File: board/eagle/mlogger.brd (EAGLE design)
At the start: 59.4 x 33.3 mm, 40 parts, among them J1 MICROSD-9P, SW1 SS-12D00G3, SW2 TVAF06-A020B-R, SW3 TVAF06-A020B-R

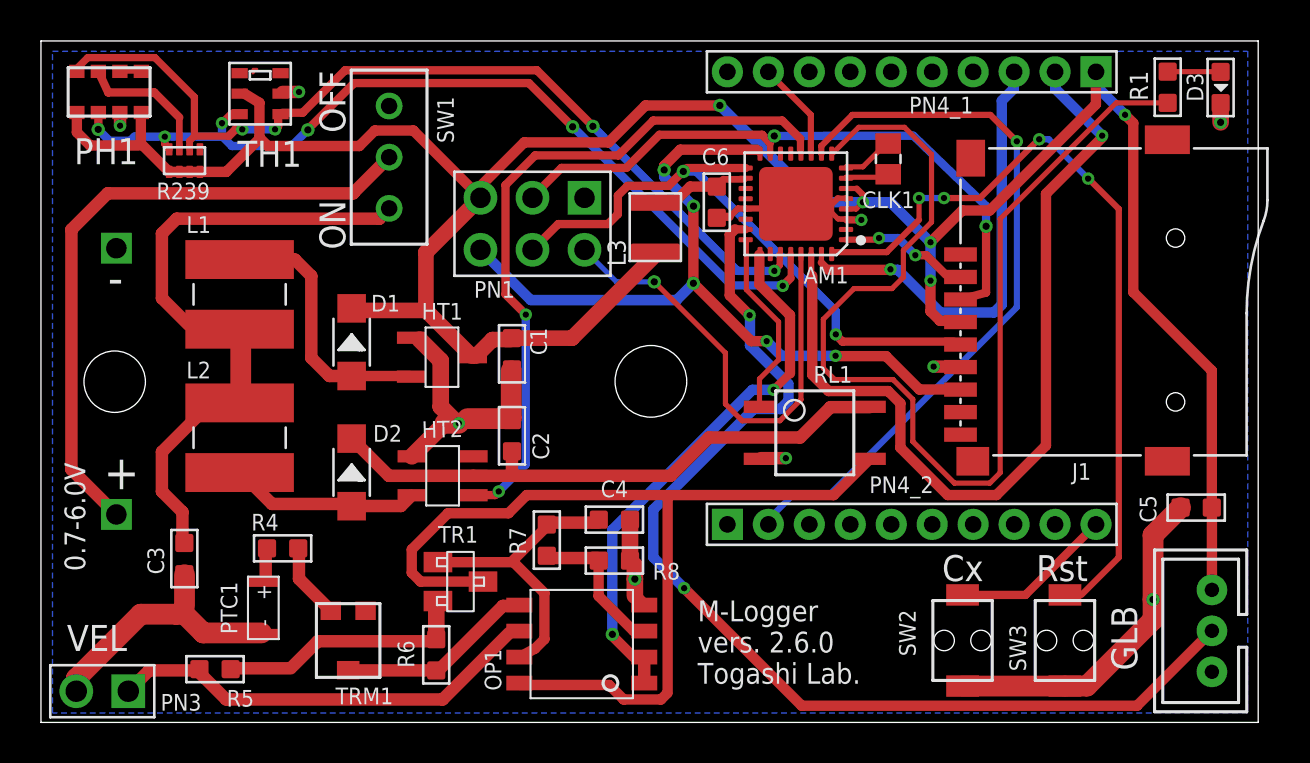
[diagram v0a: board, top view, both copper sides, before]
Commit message: AVR32DB32を使ったVersion3.0の開発開始。
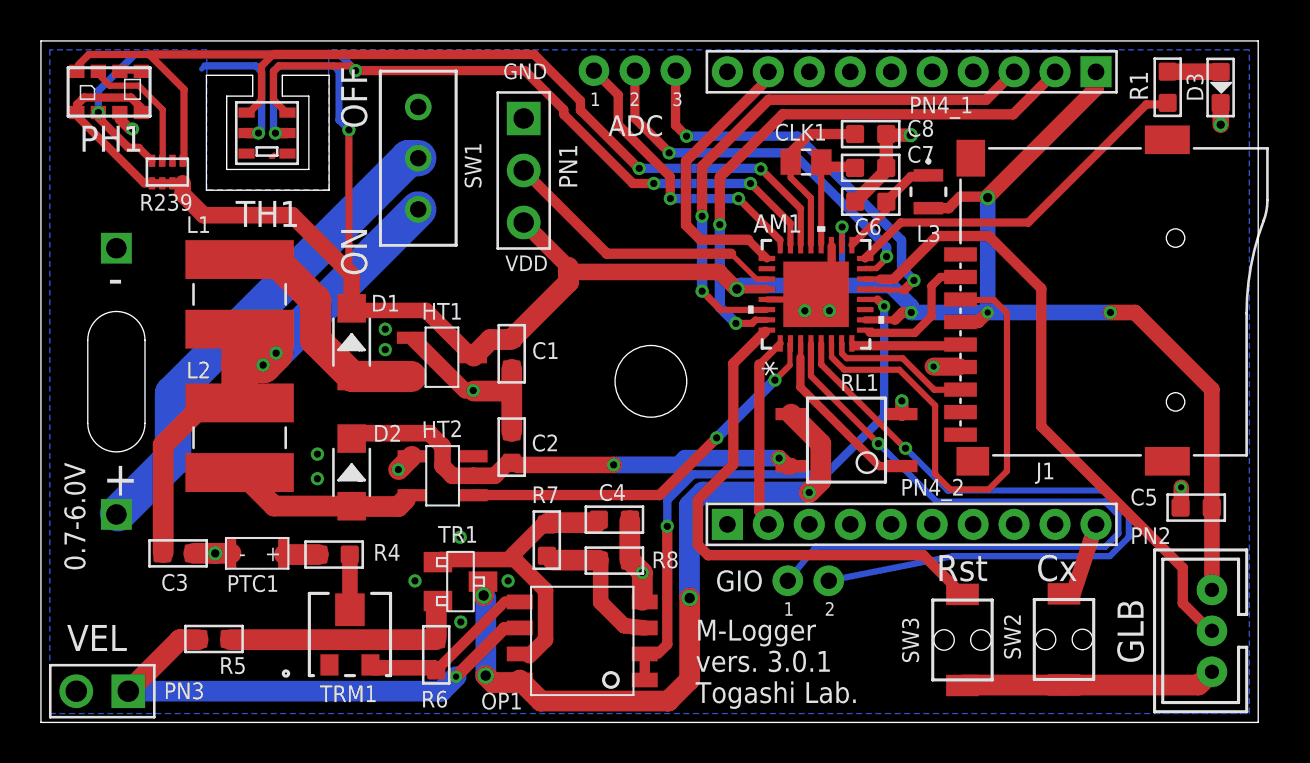
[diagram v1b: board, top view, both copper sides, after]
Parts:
- added C7, C8: (no value), MyParts:C0603
- AM1: value ATMEGA328P-MU-QFN32 -> AVR64DB32-I/RXBVQFN32_RXB_MCH; device Seeed-IC:QFN32G-0.5-5X5MM -> MyParts:VQFN32_RXB_MCH
- L3: value (none) -> LBR2012T100KIND_TAIYO_LBR2012_TAY; device MyParts:DFE322512F-100M -> MyParts:IND_TAIYO_LBR2012_TAY
- PN1: value 2x3p-2.54 -> 3p-2.54; device MyParts:H2X3-2.54 -> MyParts:H3-2.54
- TRM1: value PVZ3471C01 -> TC33X-1-103EIND_1-103E-L; device MyParts:PVZ3471C01 -> MyParts:IND_1-103E-L
- moved L3 13.4 mm to (43.3, 25.9), turned to 270 degrees
- moved C6 7.52 mm to (40.5, 25.4), turned to 90 degrees
- moved SW3 5.00 mm to (45.0, 4.03)
- moved SW2 4.95 mm to (50.0, 4.05)
- moved AM1 4.52 mm to (37.8, 20.9), turned to 90 degrees
- moved PTC1 4.24 mm to (9.28, 8.26), turned to 0 degrees
- moved CLK1 4.02 mm to (37.4, 27.4), turned to 180 degrees
- moved PN1 2.64 mm to (23.6, 26.9), turned to 0 degrees
- moved R4 2.53 mm to (14.3, 8.20)
- moved TH1 2.34 mm to (12.0, 29.8), turned to 180 degrees
- moved RL1 1.59 mm to (39.3, 13.8), turned to 90 degrees
- moved R5 1.47 mm to (8.45, 4.07)
- moved SW1 1.42 mm to (18.4, 27.5)
- moved R239 1.01 mm to (6.17, 26.9)
- moved C2 0.56 mm to (23.0, 13.4)
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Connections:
- removed net AVCC: AM1.18, C6.2, L3.2
- removed net N$17: R4.2, TRM1.P$3
- removed net N$33: AM1.1, J1.2
- removed net XTAL1: AM1.7, CLK1.2
- removed net XTAL2: AM1.8, CLK1.1
- new net N$11: AM1.15
- new net N$12: AM1.5
- new net N$13: AM1.4
- new net N$2: AM1.20, C7.1, CLK1.1
- new net N$6: AM1.21, C8.1, CLK1.2
- new net N$7: AM1.27, PN1.2
- new net N$8: AM1.13
- new net N$9: AM1.24
- new net SS: AM1.9, J1.2
- new net VREFA: AM1.17, C6.2, L3.1
- net ADC0: now also AM1.14; no longer AM1.23
- net ADC2: now also AM1.12; no longer AM1.25
- net CTS: now also AM1.1; no longer AM1.10
- net GND: now also AM1.19, AM1.29, C7.2, C8.2; no longer AM1.21, AM1.3, AM1.5
- net MISO: now also AM1.7; no longer AM1.16, PN1.4
- net MOSI: now also AM1.6; no longer AM1.15, PN1.2
- net N$1: now also R4.2, TRM1.2; no longer AM1.9, R1.2
- net N$23: now also AM1.2; no longer AM1.12
- net N$24: now also AM1.3; no longer AM1.24
- net N$4: now also AM1.16, R1.2; no longer AM1.29, PN1.6
- net P$3: now also TRM1.3; no longer TRM1.P$2
- net RXD: now also AM1.31; no longer AM1.30
- net SCK: now also AM1.8; no longer AM1.17, PN1.5
- net SCL: now also AM1.23; no longer AM1.28
- net SDA: now also AM1.22, R239.8; no longer AM1.27, R239.6
- net SLP: now also AM1.25; no longer AM1.11
- net TXD: now also AM1.30; no longer AM1.31
- net VDD: now also AM1.10, AM1.18, AM1.28, L3.2; no longer AM1.4, AM1.6, L3.1
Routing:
- net N$1: track 55.0 -> 2.70 mm
- net N$13: track 0.00 -> 37.5 mm, vias 0 -> 2
- net N$12: track 0.00 -> 35.4 mm, vias 0 -> 2
- net MISO: track 38.4 -> 7.02 mm, vias 5 -> 0
- net CTS: track 35.9 -> 9.39 mm, vias 1 -> 0
- net SCK: track 30.3 -> 5.37 mm, vias 2 -> 0
- net ADC0: track 53.1 -> 30.8 mm, vias 2 -> 0
- net N$8: track 0.00 -> 20.8 mm, vias 0 -> 3
- net N$11: track 0.00 -> 19.0 mm, vias 0 -> 3
- net N$23: track 34.0 -> 19.2 mm
- net RXD: track 42.4 -> 27.6 mm, vias 1 -> 2
- net N$9: track 0.00 -> 14.2 mm, vias 0 -> 3
- net N$7: track 0.00 -> 14.1 mm
- net N$5: track 38.8 -> 25.8 mm, vias 4 -> 0
- net P$6: track 46.4 -> 35.0 mm, vias 0 -> 4
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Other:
- outline, holes or cut-outs redrawn
- board text added: "1"
- board text added: "2"
- board text added: "3"
- board text added: "ADC"
- board text added: "AM1"
- board text added: "GIO"
- board text added: "GND"
- board text added: "M-Logger vers. 3.0.1 Togashi Lab."
- board text added: "VDD"
- board text removed: "M-Logger vers. 2.6.0 Togashi Lab."

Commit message: 基板形状微修正
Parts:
- renumbered BBOX to BB1, PN4_1 to PN4_1(XB1), PN4_2 to PN4_2(XB1)
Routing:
- net GND: vias 21 -> 19
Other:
- outline, holes or cut-outs redrawn
- board text added: "0.7- 6.0V"
- board text removed: "0.7-6.0V"
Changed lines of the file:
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@@
 <setting verticaltext="up"/>
 </settings>
-<grid distance="1" unitdist="mil" unit="mil" style="lines" multiple="1" display="yes" altdistance="1" altunitdist="mil" altunit="mil"/>
+<grid distance="0.1" unitdist="mm" unit="mm" style="lines" multiple="1" display="yes" altdistance="1" altunitdist="mil" altunit="mil"/>
 <layers>
 <layer number="1" name="Top" color="4" fill="1" visible="yes" active="yes"/>
@@
 <text x="53.8388" y="2.865" size="1.27" layer="25" font="vector" rot="R90">GLB</text>
 <text x="1.266" y="3.488" size="1.27" layer="25" font="vector">VEL</text>
-<text x="3.266" y="20.888" size="1.6764" layer="25">-</text>
-<text x="3.0152" y="11.0832" size="1.6764" layer="25">+</text>
-<text x="2.166" y="7.388" size="1.016" layer="25" font="vector" rot="R90">0.7-6.0V</text>
+<text x="1.166" y="22.188" size="2.54" layer="25">-</text>
+<text x="1.0152" y="9.3832" size="1.6764" layer="25">+</text>
+<text x="1.266" y="6.288" size="1.016" layer="25" font="vector">0.7-
+6.0V</text>
 <polygon width="0.0762" layer="21">
 <vertex x="57.1246" y="31.242"/>
@@
 <wire x1="4.8514" y1="30.4292" x2="4.0894" y2="30.4292" width="0.0762" layer="21"/>
 <wire x1="4.0894" y1="30.4292" x2="4.0894" y2="31.3944" width="0.0762" layer="21"/>
+<wire x1="17.3" y1="8.8" x2="18.3" y2="9.8" width="0" layer="20" curve="-90"/>
+<wire x1="18.3" y1="9.8" x2="21.3" y2="9.8" width="0" layer="20"/>
+<wire x1="21.3" y1="9.8" x2="21.3" y2="8.8" width="0" layer="20" curve="-180"/>
+<wire x1="18.3" y1="8.8" x2="21.3" y2="8.8" width="0" layer="20"/>
+<wire x1="17.3" y1="7.2" x2="18.3" y2="7.2" width="0" layer="20" curve="180"/>
+<wire x1="17.3" y1="7.2" x2="17.3" y2="8.8" width="0" layer="20"/>
+<wire x1="18.3" y1="7.2" x2="18.3" y2="8.8" width="0" layer="20"/>
+<wire x1="32.5" y1="32.8" x2="52.5" y2="32.8" width="0.1524" layer="22"/>
+<wire x1="52.5" y1="32.8" x2="52.5" y2="30.8" width="0.1524" layer="22"/>
+<wire x1="52.5" y1="30.8" x2="32.5" y2="30.8" width="0.1524" layer="22"/>
+<wire x1="32.5" y1="30.8" x2="32.5" y2="32.8" width="0.1524" layer="22"/>
+<wire x1="32.5" y1="10.7" x2="52.5" y2="10.7" width="0.1524" layer="22"/>
+<wire x1="52.5" y1="10.7" x2="52.5" y2="8.7" width="0.1524" layer="22"/>
+<wire x1="52.5" y1="8.7" x2="32.5" y2="8.7" width="0.1524" layer="22"/>
+<wire x1="32.5" y1="8.7" x2="32.5" y2="10.7" width="0.1524" layer="22"/>
 </plain>
 <attributes>
@@
 <attribute name="NAME" x="15.805" y="17.677" size="0.381" layer="33" ratio="10" rot="R90"/>
 </element>
-<element name="PN4_1" library="OPL_Connector" library_urn="urn:adsk.eagle:library:8004395" package="H10-2.0" package3d_urn="urn:adsk.eagle:package:8004550/1" value="10p-2.0" x="42.517059375" y="31.767771875" locked="yes" smashed="yes" rot="R270" grouprefs="XBEE">
+<element name="PN4_1(XB1)" library="OPL_Connector" library_urn="urn:adsk.eagle:library:8004395" package="H10-2.0" package3d_urn="urn:adsk.eagle:package:8004550/1" value="10p-2.0" x="42.517059375" y="31.767771875" locked="yes" smashed="yes" rot="R270" grouprefs="XBEE">
 <attribute name="MPN" value="F243-1110A1BSUA1" x="42.517059375" y="31.767771875" locked="yes" size="1.778" layer="27" rot="R270" display="off"/>
 <attribute name="NAME" x="40.104059375" y="31.259771875" locked="yes" size="1.016" layer="33" ratio="10"/>
-<attribute name="NAME" x="42.390059375" y="29.735771875" locked="yes" size="0.8128" layer="25" ratio="11"/>
-</element>
-<element name="PN4_2" library="OPL_Connector" library_urn="urn:adsk.eagle:library:8004395" package="H10-2.0" package3d_urn="urn:adsk.eagle:package:8004550/1" value="10p-2.0" x="42.517059375" y="9.669771875" locked="yes" smashed="yes" rot="R90" grouprefs="XBEE">
+<attribute name="NAME" x="37.390059375" y="29.735771875" locked="yes" size="0.8128" layer="25" ratio="11"/>
+</element>
+<element name="PN4_2(XB1)" library="OPL_Connector" library_urn="urn:adsk.eagle:library:8004395" package="H10-2.0" package3d_urn="urn:adsk.eagle:package:8004550/1" value="10p-2.0" x="42.517059375" y="9.669771875" locked="yes" smashed="yes" rot="R90" grouprefs="XBEE">
 <attribute name="MPN" value="F243-1110A1BSUA1" x="22.197059375" y="2.049771875" locked="yes" size="1.778" layer="27" rot="R90" display="off"/>
 <attribute name="NAME" x="41.970059375" y="11.072771875" locked="yes" size="0.8128" layer="25" ratio="11"/>
@@
 </element>
 <element name="TR1" library="MyParts" package="MMBTA42" value="MMBTA42" x="19.384" y="7.826" smashed="yes" rot="R270">
-<attribute name="NAME" x="19.392" y="8.774" size="0.8128" layer="25"/>
+<attribute name="NAME" x="21.592" y="7.774" size="0.8128" layer="25"/>
 </element>
 <element name="OP1" library="MyParts" package="NJM4565" value="NJM4565" x="29.4814" y="2.0724" smashed="yes" rot="R90">
@@
 <attribute name="NAME" x="9.072" y="6.3754" size="0.8128" layer="25"/>
 </element>
-<element name="BBOX" library="MyParts" package="BH321" value="BH321" x="59.182" y="0.254" smashed="yes" rot="MR0">
-<attribute name="NAME" x="33.42" y="19.318" size="1.778" layer="26" rot="MR0"/>
+<element name="BB1" library="MyParts" package="BH321" value="BH321" x="59.182" y="0.254" smashed="yes" rot="MR0">
+<attribute name="NAME" x="31.92" y="20.718" size="1.778" layer="26" rot="MR0"/>
 </element>
 <element name="PN3" library="MyParts" package="H2-2.54" package3d_urn="urn:adsk.eagle:package:8004540/1" value="2p-2.54" x="2.994" y="1.524" smashed="yes" rot="R270">
@@
 </element>
 <element name="R4" library="MyParts" package="R0603" package3d_urn="urn:adsk.eagle:package:8004941/1" value="" x="14.3146" y="8.1952" smashed="yes" rot="R90">
-<attribute name="NAME" x="16.2278" y="7.898" size="0.8128" layer="25" ratio="11"/>
+<attribute name="NAME" x="12.9278" y="9.098" size="0.8128" layer="25" ratio="11"/>
 <attribute name="VALUE" x="15.9196" y="9.6302" size="0.635" layer="27" ratio="10" rot="R180"/>
 </element>
@@
 <signals>
 <signal name="GND" class="1">
-<contactref element="PN4_1" pad="10"/>
+<contactref element="PN4_1(XB1)" pad="10"/>
 <contactref element="HT1" pad="P$1"/>
 <contactref element="OP1" pad="P$4"/>
 <contactref element="HT2" pad="P$4"/>
 <contactref element="PTC1" pad="P$1"/>
-<contactref element="BBOX" pad="V-"/>
+<contactref element="BB1" pad="V-"/>
 <contactref element="PN3" pad="2"/>
 <contactref element="RL1" pad="GND"/>
@@
 <wire x1="7.99558125" y1="32.0548" x2="7.84318125" y2="31.9024" width="0.254" layer="16"/>
 <via x="20.4978" y="4.9022" extent="1-16" drill="0.35"/>
-<via x="20.4724" y="9.0424" extent="1-16" drill="0.35"/>
-<via x="18.2626" y="6.9088" extent="1-16" drill="0.35"/>
 <via x="22.8092" y="6.9088" extent="1-16" drill="0.35"/>
 <via x="16.8116" y="19.2" extent="1-16" drill="0.35"/>
@@
 </signal>
 <signal name="VDD" class="2">
-<contactref element="PN4_1" pad="1"/>
+<contactref element="PN4_1(XB1)" pad="1"/>
 <contactref element="HT1" pad="P$3"/>
 <contactref element="D1" pad="-"/>
@@
 </signal>
 <signal name="RXD">
-<contactref element="PN4_1" pad="2"/>
+<contactref element="PN4_1(XB1)" pad="2"/>
 <contactref element="AM1" pad="31"/>
 <wire x1="47.4726" y1="29.6926" x2="36.2204" y2="29.6926" width="0.508" layer="1"/>
@@
 </signal>
 <signal name="TXD">
-<contactref element="PN4_1" pad="3"/>
+<contactref element="PN4_1(XB1)" pad="3"/>
 <contactref element="AM1" pad="30"/>
 <wire x1="47.517059375" y1="31.767771875" x2="46.1530875" y2="30.4038" width="0.508" layer="1"/>
@@
 </signal>
 <signal name="SLP">
-<contactref element="PN4_1" pad="9"/>
+<contactref element="PN4_1(XB1)" pad="9"/>
 <contactref element="AM1" pad="25"/>
 <wire x1="31.496" y1="24.2824" x2="32.2098" y2="23.5686" width="0.508" layer="1"/>
@@
 </signal>
 <signal name="CTS">
-<contactref element="PN4_2" pad="2"/>
+<contactref element="PN4_2(XB1)" pad="2"/>
 <contactref element="AM1" pad="1"/>
 <wire x1="35.0774" y1="17.4853" x2="35.0774" y2="10.298075" width="0.508" layer="1"/>
@@
 </signal>
 <signal name="N$3">
-<contactref element="PN4_2" pad="10"/>
+<contactref element="PN4_2(XB1)" pad="10"/>
 <contactref element="SW2" pad="P$1"/>
 <wire x1="49.953" y1="6.2758" x2="50.39806875" y2="6.2758" width="0.254" layer="1"/>
@@
 </signal>
 <signal name="VBT">
-<contactref element="BBOX" pad="V+"/>
+<contactref element="BB1" pad="V+"/>
 <contactref element="SW1" pad="P$2"/>
 <wire x1="18.4224" y1="27.5492" x2="17.948" y2="27.5492" width="1.778" layer="16"/>
